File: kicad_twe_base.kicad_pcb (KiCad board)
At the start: 2 copper layers, 72 x 47.5 mm, 10 parts, among them J3 Conn_01x07, SW1 SW_SPDT, SW2 SW_Push, SW3 SW_SPDT, U1 TWE-L-DP-W

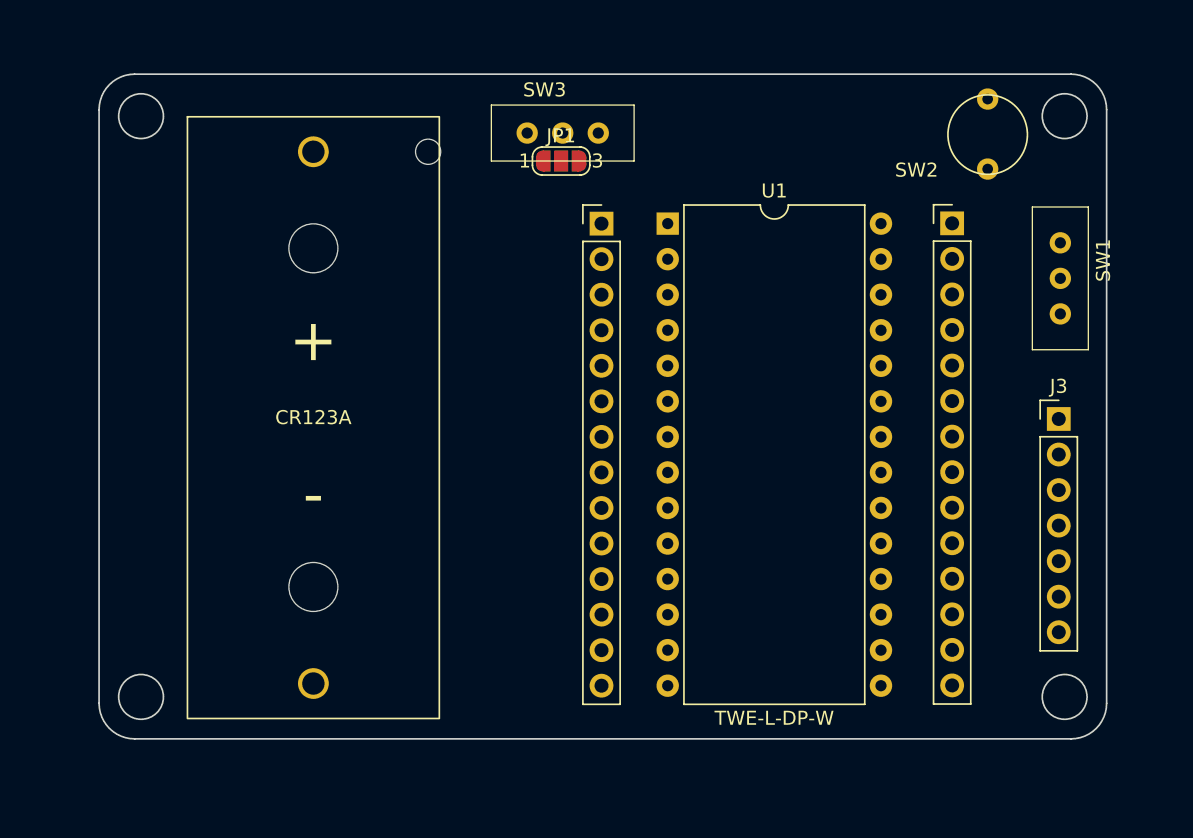
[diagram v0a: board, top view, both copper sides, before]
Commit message: シルク変更途中
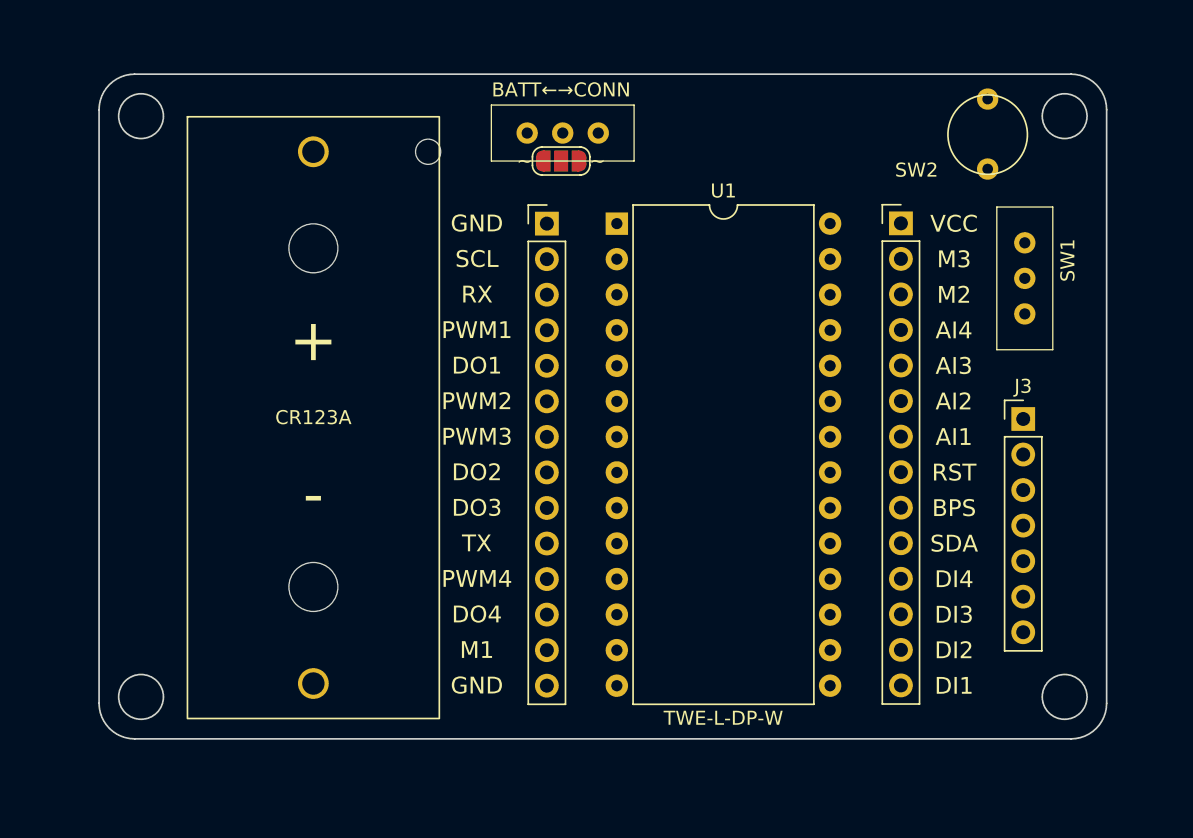
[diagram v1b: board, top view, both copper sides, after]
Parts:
- moved ~ 3.91 mm to (32.0, -36.8)
- moved ~ 3.66 mm to (57.3, -36.8)
- moved U1 3.63 mm to (37.0, -36.8)
- moved J3 2.54 mm to (66.0, -22.9)
- moved SW1 2.54 mm to (64.2, -38.0)
- renumbered SW3 to BATT←→CONN, JP1 to ~
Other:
- board text added: "AI1"
- board text added: "AI2"
- board text added: "AI3"
- board text added: "AI4"
- board text added: "BPS"
- board text added: "DI1"
- board text added: "DI2"
- board text added: "DI3"
- board text added: "DI4"
- board text added: "DO1"
- board text added: "DO2"
- board text added: "DO3"
- board text added: "DO4"
- board text added: "GND"
- board text added: "M1"
- board text added: "M2"
- board text added: "M3"
- board text added: "PWM1"
- board text added: "PWM2"
- board text added: "PWM3"
- board text added: "PWM4"
- board text added: "RST"
- board text added: "RX"
- board text added: "SCL"
- board text added: "SDA"
- board text added: "TX"
- board text added: "VCC"
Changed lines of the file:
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@@
   (net 31 "unconnected-(SW1-Pad1)")
   (footprint "Connector_PinHeader_2.54mm:PinHeader_1x14_P2.54mm_Vertical" (layer "F.Cu")
-    (at 60.96 -36.84)
+    (at 57.3 -36.84)
     (descr "Through hole straight pin header, 1x14, 2.54mm pitch, single row")
     (tags "Through hole pin header THT 1x14 2.54mm single row")
@@
   )
   (footprint "Package_DIP:DIP-28_W15.24mm" (layer "F.Cu")
-    (at 40.635 -36.82)
+    (at 37 -36.82)
     (descr "28-lead though-hole mounted DIP package, row spacing 15.24 mm (600 mils)")
     (tags "THT DIP DIL PDIP 2.54mm 15.24mm 600mil")
@@
   )
   (footprint "Connector_PinHeader_2.54mm:PinHeader_1x07_P2.54mm_Vertical" (layer "F.Cu")
-    (at 68.58 -22.86)
+    (at 66.04 -22.86)
     (descr "Through hole straight pin header, 1x07, 2.54mm pitch, single row")
     (tags "Through hole pin header THT 1x07 2.54mm single row")
@@
       (effects (font (size 1 1) (thickness 0.15)))
     )
-    (fp_text value "Conn_01x07" (at 0 17.57) (layer "F.Fab")
+    (fp_text value "Conn_01x07" (at -0.9 17.57) (layer "F.Fab")
       (effects (font (size 1 1) (thickness 0.15)))
     )
@@
   )
   (footprint "Connector_PinHeader_2.54mm:PinHeader_1x14_P2.54mm_Vertical" (layer "F.Cu")
-    (at 35.905 -36.82)
+    (at 32 -36.82)
     (descr "Through hole straight pin header, 1x14, 2.54mm pitch, single row")
     (tags "Through hole pin header THT 1x14 2.54mm single row")
@@
     (property "Sheetname" "")
     (attr through_hole)
-    (fp_text reference "SW3" (at 3.81 -5.08) (layer "F.SilkS")
+    (fp_text reference "BATT←→CONN" (at 4.9875 -5.08) (layer "F.SilkS")
       (effects (font (size 1 1) (thickness 0.15)))
     )
@@
   )
   (footprint "KICAD_MYLIB:SW_SLIDE_sengoku" (layer "F.Cu")
-    (at 66.6925 -38.0075 -90)
+    (at 64.1525 -38.0075 -90)
     (property "Sheetfile" "kicad_twe_base.kicad_sch")
     (property "Sheetname" "")
@@
     (property "Sheetname" "")
     (attr exclude_from_pos_files)
-    (fp_text reference "JP1" (at 0 -1.8) (layer "F.SilkS")
+    (fp_text reference "~" (at 0 -1.8) (layer "F.SilkS")
       (effects (font (size 1 1) (thickness 0.15)))
     )
@@
       (effects (font (size 1 1) (thickness 0.15)))
     )
-    (fp_text user "1" (at -2.6 0) (layer "F.SilkS")
-      (effects (font (size 1 1) (thickness 0.15)))
-    )
-    (fp_text user "3" (at 2.6 0) (layer "F.SilkS")
+    (fp_text user "~" (at -2.6 0) (layer "F.SilkS")
+      (effects (font (size 1 1) (thickness 0.15)))
+    )
+    (fp_text user "~" (at 2.6 0) (layer "F.SilkS")
       (effects (font (size 1 1) (thickness 0.15)))
     )
@@
       ))
   )
+  (gr_text "BPS" (at 61.1 -16.48) (layer "F.SilkS")
+    (effects (font (size 1.2 1.2) (thickness 0.1)))
+  )
+  (gr_text "PWM1" (at 27 -29.2) (layer "F.SilkS")
+    (effects (font (size 1.2 1.2) (thickness 0.1)))
+  )
+  (gr_text "AI3" (at 61.1 -26.64) (layer "F.SilkS")
+    (effects (font (size 1.2 1.2) (thickness 0.1)))
+  )
+  (gr_text "SCL" (at 27 -34.28) (layer "F.SilkS")
+    (effects (font (size 1.2 1.2) (thickness 0.1)))
+  )
+  (gr_text "AI1" (at 61.1 -21.56) (layer "F.SilkS")
+    (effects (font (size 1.2 1.2) (thickness 0.1)))
+  )
+  (gr_text "PWM2" (at 27 -24.12) (layer "F.SilkS")
+    (effects (font (size 1.2 1.2) (thickness 0.1)))
+  )
+  (gr_text "VCC" (at 61.1 -36.8) (layer "F.SilkS")
+    (effects (font (size 1.2 1.2) (thickness 0.1)))
+  )
+  (gr_text "DO3" (at 27 -16.5) (layer "F.SilkS")
+    (effects (font (size 1.2 1.2) (thickness 0.1)))
+  )
+  (gr_text "TX" (at 27 -13.96) (layer "F.SilkS")
+    (effects (font (size 1.2 1.2) (thickness 0.1)))
+  )
+  (gr_text "SDA" (at 61.1 -13.94) (layer "F.SilkS")
+    (effects (font (size 1.2 1.2) (thickness 0.1)))
+  )
+  (gr_text "DI4" (at 61.1 -11.4) (layer "F.SilkS")
+    (effects (font (size 1.2 1.2) (thickness 0.1)))
+  )
+  (gr_text "RX" (at 27 -31.74) (layer "F.SilkS")
+    (effects (font (size 1.2 1.2) (thickness 0.1)))
+  )
+  (gr_text "GND" (at 27 -36.82) (layer "F.SilkS")
+    (effects (font (size 1.2 1.2) (thickness 0.1)))
+  )
+  (gr_text "DO4" (at 27 -8.88) (layer "F.SilkS")
+    (effects (font (size 1.2 1.2) (thickness 0.1)))
+  )
+  (gr_text "GND" (at 27 -3.8) (layer "F.SilkS")
+    (effects (font (size 1.2 1.2) (thickness 0.1)))
+  )
+  (gr_text "AI2" (at 61.1 -24.1) (layer "F.SilkS")
+    (effects (font (size 1.2 1.2) (thickness 0.1)))
+  )
+  (gr_text "M1" (at 27 -6.34) (layer "F.SilkS")
+    (effects (font (size 1.2 1.2) (thickness 0.1)))
+  )
+  (gr_text "M3" (at 61.1 -34.26) (layer "F.SilkS")
+    (effects (font (size 1.2 1.2) (thickness 0.1)))
+  )
+  (gr_text "RST" (at 61.1 -19.02) (layer "F.SilkS")
+    (effects (font (size 1.2 1.2) (thickness 0.1)))
+  )
+  (gr_text "DI3" (at 61.1 -8.86) (layer "F.SilkS")
+    (effects (font (size 1.2 1.2) (thickness 0.1)))
+  )
+  (gr_text "AI4" (at 61.1 -29.18) (layer "F.SilkS")
+    (effects (font (size 1.2 1.2) (thickness 0.1)))
+  )
+  (gr_text "PWM3" (at 27 -21.58) (layer "F.SilkS")
+    (effects (font (size 1.2 1.2) (thickness 0.1)))
+  )
+  (gr_text "DI1" (at 61.1 -3.78) (layer "F.SilkS")
+    (effects (font (size 1.2 1.2) (thickness 0.1)))
+  )
+  (gr_text "DO2" (at 27 -19.04) (layer "F.SilkS")
+    (effects (font (size 1.2 1.2) (thickness 0.1)))
+  )
+  (gr_text "PWM4" (at 27 -11.42) (layer "F.SilkS")
+    (effects (font (size 1.2 1.2) (thickness 0.1)))
+  )
+  (gr_text "DI2" (at 61.1 -6.32) (layer "F.SilkS")
+    (effects (font (size 1.2 1.2) (thickness 0.1)))
+  )
+  (gr_text "M2" (at 61.1 -31.72) (layer "F.SilkS")
+    (effects (font (size 1.2 1.2) (thickness 0.1)))
+  )
+  (gr_text "DO1" (at 27 -26.66) (layer "F.SilkS")
+    (effects (font (size 1.2 1.2) (thickness 0.1)))
+  )
 )

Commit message: 仮配置完了
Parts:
- moved RST 5.68 mm to (58.4, -43.2), turned to 0 degrees
- renumbered SW2 to RST, SW1 to RUN←→PRG, J3 to ~
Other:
- board text added: "PRG"
- board text added: "RXD"
- board text added: "SET"
- board text added: "TXD"
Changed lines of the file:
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@@
     (property "Sheetname" "")
     (attr through_hole)
-    (fp_text reference "J3" (at 0 -2.33) (layer "F.SilkS")
+    (fp_text reference "~" (at 0 -2.33) (layer "F.SilkS")
       (effects (font (size 1 1) (thickness 0.15)))
     )
@@
     (property "Sheetname" "")
     (attr through_hole)
-    (fp_text reference "SW1" (at 3.81 -5.08 90) (layer "F.SilkS")
+    (fp_text reference "RUN←→PRG" (at 5.0075 -4.8475 -90 unlocked) (layer "F.SilkS")
       (effects (font (size 1 1) (thickness 0.15)))
     )
@@
   )
   (footprint "KICAD_MYLIB:SW_PUSH_2pin" (layer "F.Cu")
-    (at 63.5 -45.72 -90)
-    (property "Sheetfile" "kicad_twe_base.kicad_sch")
-    (property "Sheetname" "")
-    (attr through_hole)
-    (fp_text reference "SW2" (at 5.08 5.08 180) (layer "F.SilkS")
-      (effects (font (size 1 1) (thickness 0.15)))
-    )
-    (fp_text value "SW_Push" (at 5.08 -5.08 90) (layer "F.Fab")
+    (at 58.42 -43.18)
+    (property "Sheetfile" "kicad_twe_base.kicad_sch")
+    (property "Sheetname" "")
+    (attr through_hole)
+    (fp_text reference "RST" (at 7.62 2.54 180) (layer "F.SilkS")
+      (effects (font (size 1 1) (thickness 0.15)))
+    )
+    (fp_text value "SW_Push" (at 5.08 -5.08) (layer "F.Fab")
       (effects (font (size 1 1) (thickness 0.15)))
     )
     (fp_circle (center 2.54 0) (end 5.08 1.27) (layer "F.SilkS") (width 0.12) (fill none))
-    (pad "1" thru_hole circle locked (at 0 0 270) (size 1.524 1.524) (drill 0.762) (layers *.Cu *.Mask)
+    (pad "1" thru_hole circle locked (at 0 0) (size 1.524 1.524) (drill 0.762) (layers *.Cu *.Mask)
       (net 21 "Net-(J2-Pad8)") (pinfunction "1") (pintype "passive"))
-    (pad "2" thru_hole circle locked (at 5 0 270) (size 1.524 1.524) (drill 0.762) (layers *.Cu *.Mask)
+    (pad "2" thru_hole circle locked (at 5 0) (size 1.524 1.524) (drill 0.762) (layers *.Cu *.Mask)
       (net 30 "Net-(SW1-Pad3)") (pinfunction "2") (pintype "passive"))
   )
@@
     (effects (font (size 1.2 1.2) (thickness 0.1)))
   )
+  (gr_text "VCC" (at 69.7 -10) (layer "F.SilkS")
+    (effects (font (size 1.2 1.2) (thickness 0.1)))
+  )
   (gr_text "SCL" (at 27 -34.28) (layer "F.SilkS")
     (effects (font (size 1.2 1.2) (thickness 0.1)))
@@
     (effects (font (size 1.2 1.2) (thickness 0.1)))
   )
+  (gr_text "GND" (at 69.7 -22.7) (layer "F.SilkS")
+    (effects (font (size 1.2 1.2) (thickness 0.1)))
+  )
   (gr_text "VCC" (at 61.1 -36.8) (layer "F.SilkS")
     (effects (font (size 1.2 1.2) (thickness 0.1)))
@@
     (effects (font (size 1.2 1.2) (thickness 0.1)))
   )
+  (gr_text "TXD" (at 69.7 -20.16) (layer "F.SilkS")
+    (effects (font (size 1.2 1.2) (thickness 0.1)))
+  )
   (gr_text "SDA" (at 61.1 -13.94) (layer "F.SilkS")
     (effects (font (size 1.2 1.2) (thickness 0.1)))
@@
     (effects (font (size 1.2 1.2) (thickness 0.1)))
   )
+  (gr_text "RXD" (at 69.7 -15.08) (layer "F.SilkS")
+    (effects (font (size 1.2 1.2) (thickness 0.1)))
+  )
   (gr_text "RX" (at 27 -31.74) (layer "F.SilkS")
     (effects (font (size 1.2 1.2) (thickness 0.1)))
@@
     (effects (font (size 1.2 1.2) (thickness 0.1)))
   )
+  (gr_text "RST" (at 69.7 -12.54) (layer "F.SilkS")
+    (effects (font (size 1.2 1.2) (thickness 0.1)))
+  )
   (gr_text "GND" (at 27 -3.8) (layer "F.SilkS")
     (effects (font (size 1.2 1.2) (thickness 0.1)))
@@
     (effects (font (size 1.2 1.2) (thickness 0.1)))
   )
+  (gr_text "PRG" (at 69.7 -17.62) (layer "F.SilkS")
+    (effects (font (size 1.2 1.2) (thickness 0.1)))
+  )
+  (gr_text "SET" (at 69.7 -7.46) (layer "F.SilkS")
+    (effects (font (size 1.2 1.2) (thickness 0.1)))
+  )

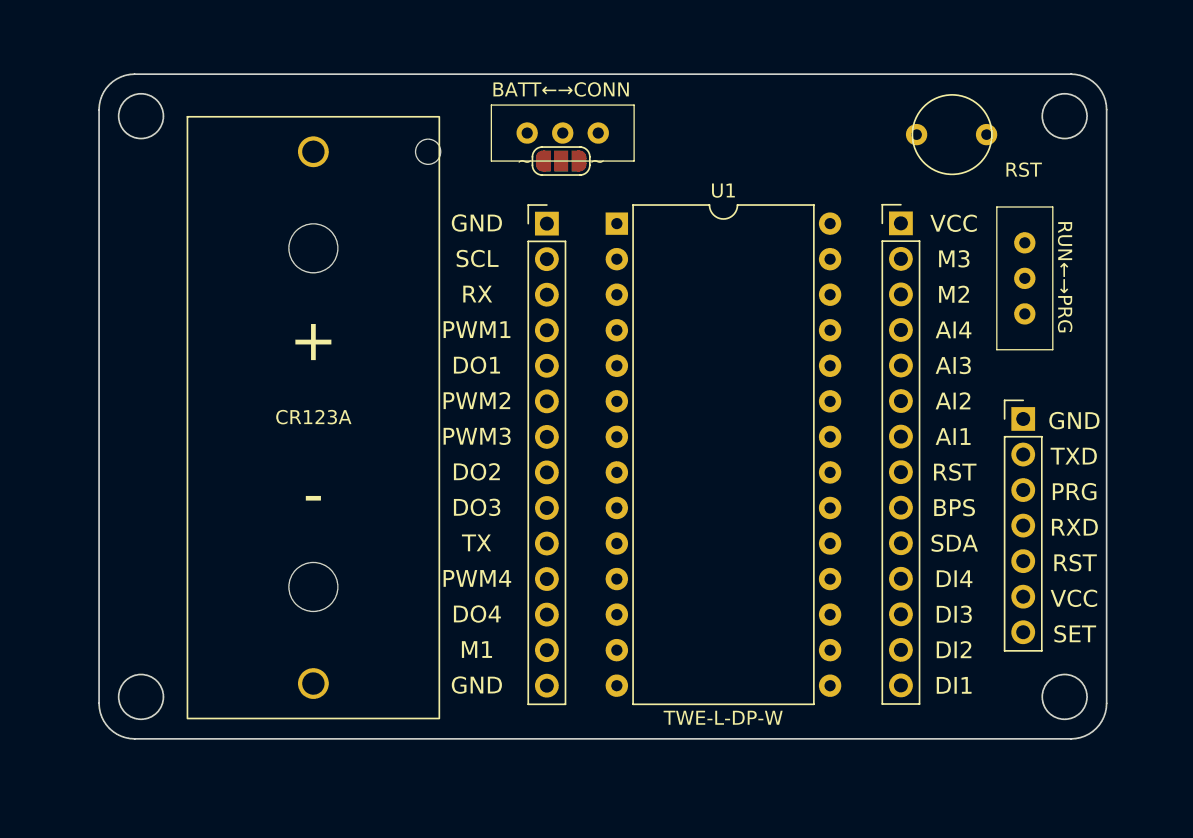
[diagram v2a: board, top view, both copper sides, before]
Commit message: プルアップ抵抗抵抗仮配置
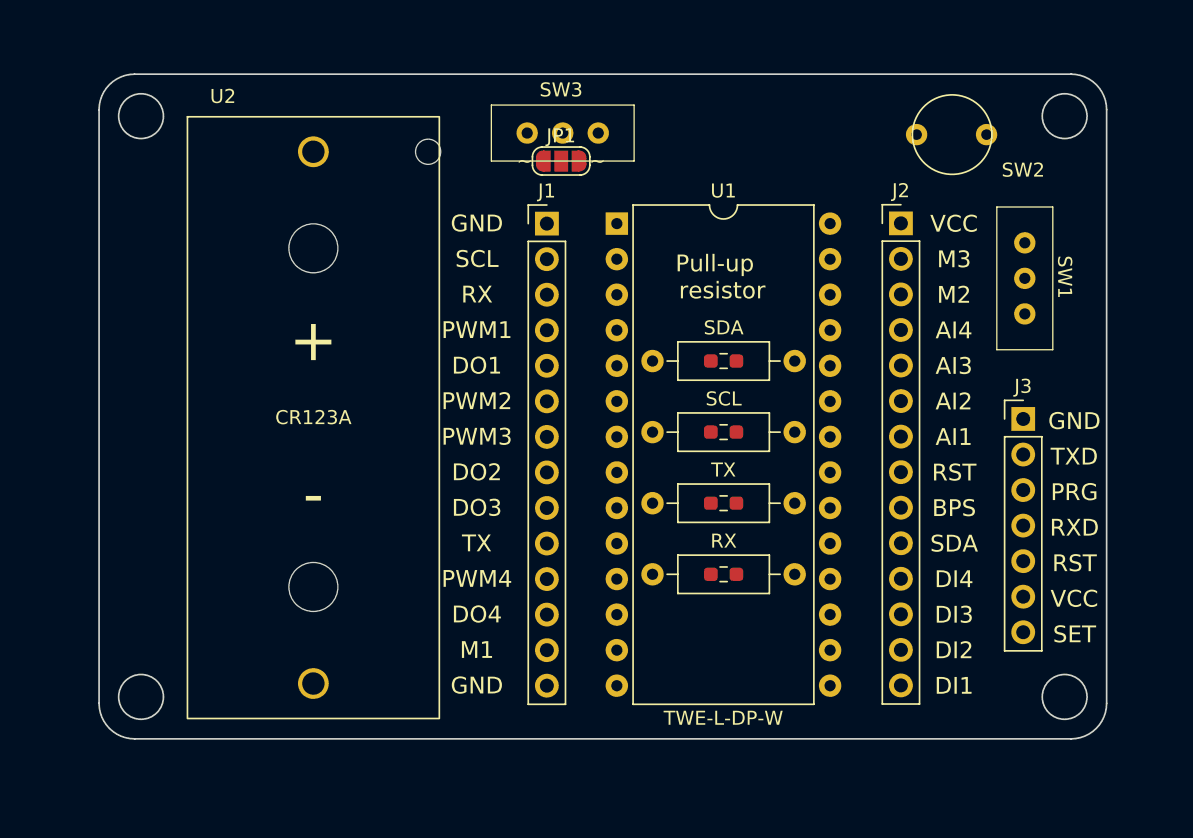
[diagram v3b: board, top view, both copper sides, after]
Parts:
- added RX: ~, Resistor_THT:R_Axial_DIN0207_L6.3mm_D2.5mm_P10.16mm_Horizontal, F.Cu at (39.5, -11.8)
- added SCL: ~, Resistor_THT:R_Axial_DIN0207_L6.3mm_D2.5mm_P10.16mm_Horizontal, F.Cu at (39.5, -21.9)
- added SDA: ~, Resistor_THT:R_Axial_DIN0207_L6.3mm_D2.5mm_P10.16mm_Horizontal, F.Cu at (39.5, -27.0)
- added TX: ~, Resistor_THT:R_Axial_DIN0207_L6.3mm_D2.5mm_P10.16mm_Horizontal, F.Cu at (39.5, -16.8)
- added ~: ~, Resistor_SMD:R_0603_1608Metric_Pad0.98x0.95mm_HandSolder, F.Cu at (44.6, -11.8)
- added ~: ~, Resistor_SMD:R_0603_1608Metric_Pad0.98x0.95mm_HandSolder, F.Cu at (44.6, -16.8)
- added ~: ~, Resistor_SMD:R_0603_1608Metric_Pad0.98x0.95mm_HandSolder, F.Cu at (44.6, -21.9)
- added ~: ~, Resistor_SMD:R_0603_1608Metric_Pad0.98x0.95mm_HandSolder, F.Cu at (44.6, -27.0)
- J1, J2: renamed from ~; value Conn_01x14 -> ~
- J3: renamed from ~; value Conn_01x07 -> ~
- JP1: renamed from ~; value SolderJumper_3_Open -> ~
- SW1: renamed from RUN←→PRG; value SW_SPDT -> ~
- SW2: renamed from RST; value SW_Push -> ~
- SW3: renamed from BATT←→CONN; value SW_SPDT -> ~
- U2: renamed from ~; value BHC-CR123A -> ~
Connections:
- net Net-(J2-Pad1) renamed +3V3
- J1 pad 1: Net-(J1-Pad1) -> GND
- J1 pad 14: Net-(J1-Pad1) -> GND
- J3 pad 1: Net-(J1-Pad1) -> GND
- SW1 pad 3: Net-(SW1-Pad3) -> GND
- SW2 pad 2: Net-(SW1-Pad3) -> GND
- U1 pad 1: Net-(J1-Pad1) -> GND
- U1 pad 14: Net-(J1-Pad1) -> GND
- U2 pad 2: Net-(J1-Pad1) -> GND
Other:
- board text added: "Pull-up resistor"
